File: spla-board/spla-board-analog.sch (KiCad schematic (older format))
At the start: 38 parts, among them J13 J_ANALOG, J14 J_AREF, U4 ADC1173, U5 ADC1173, U6 ADC1173

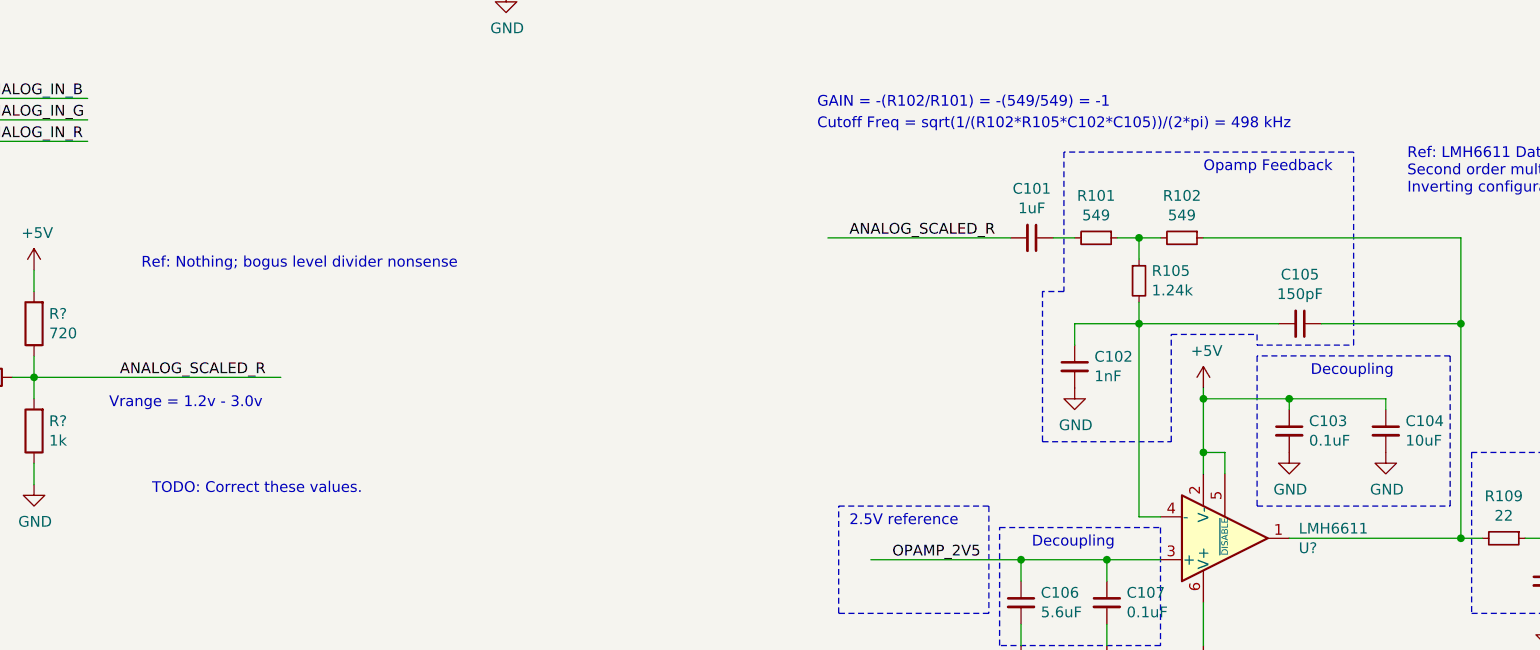
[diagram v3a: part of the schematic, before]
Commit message: schematic: More opamp fiddling.
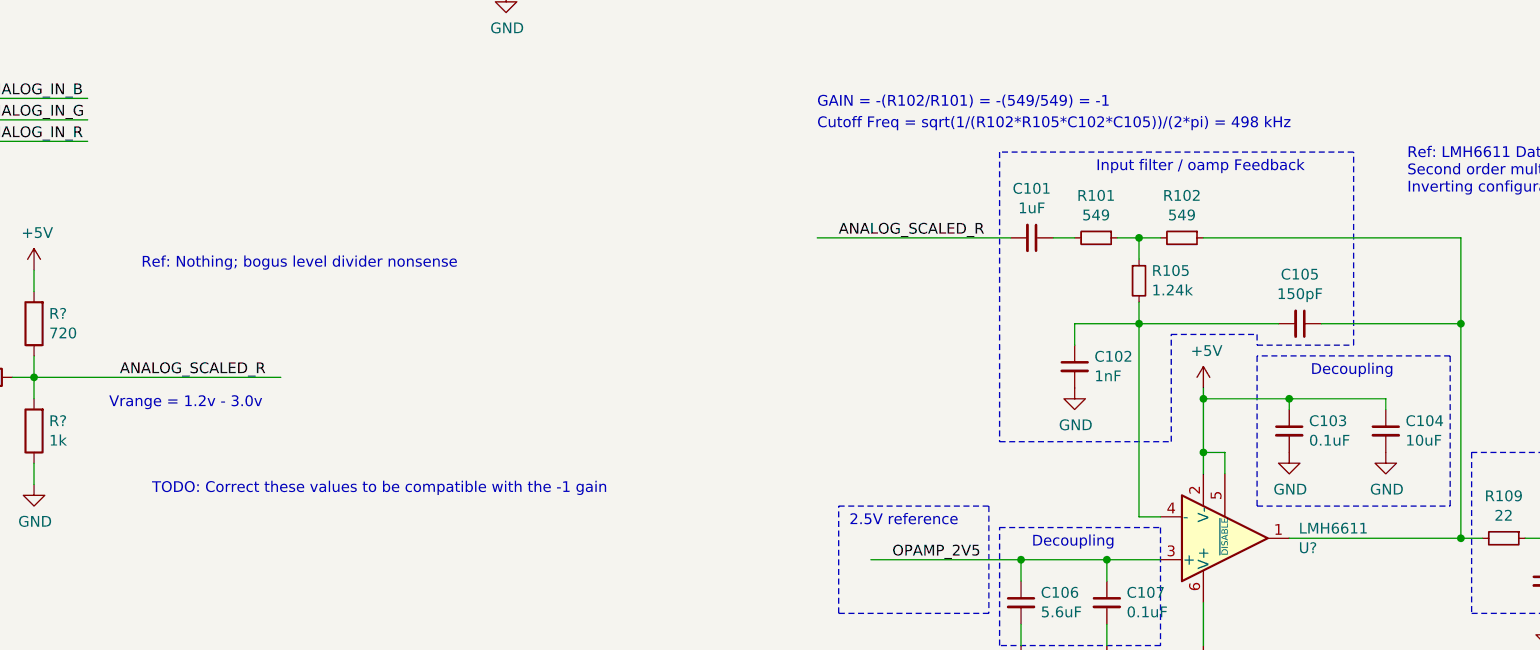
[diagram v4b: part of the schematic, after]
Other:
- note added: "Input filter / oamp Feedback"
- note added: "TODO: Correct these values to be compatible with the -1 gain"
- note removed: "Opamp Feedback"
- note removed: "TODO: Correct these values."
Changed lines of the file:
@@
 Wire Wire Line
 	9800 5650 9800 5550
-Text Label 6550 3850 0    50   ~ 0
+Text Label 6500 3850 0    50   ~ 0
 ANALOG_SCALED_R
 Wire Wire Line
-	6450 3850 7300 3850
+	6400 3850 7300 3850
 Wire Wire Line
 	7500 3850 7600 3850
@@
 	12450 2300 12450 2400
 Text Notes 3300 5050 0    50   ~ 0
-TODO: Correct these values.
+TODO: Correct these values to be compatible with the -1 gain
 Text Notes 7850 2350 0    50   ~ 0
 TODO: Inject opamps to maintain levels
@@
 Cutoff Freq = sqrt(1/(R102*R105*C102*C105))/(2*pi) = 498 kHz
 Wire Notes Line
-	7550 3450 7550 4100
-Wire Notes Line
-	7550 4100 7450 4100
-Wire Notes Line
-	7450 4100 7450 4800
-Wire Notes Line
-	7450 4800 8050 4800
+	7250 4800 8050 4800
 Wire Notes Line
 	8050 4800 8050 4300
@@
 	8900 4350 8900 3450
 Wire Notes Line
-	8900 3450 7550 3450
-Text Notes 8200 3550 0    50   ~ 0
-Opamp Feedback
+	8900 3450 7250 3450
+Text Notes 7700 3550 0    50   ~ 0
+Input filter / oamp Feedback
+Wire Notes Line
+	7250 3450 7250 4800
 $EndSCHEMATC

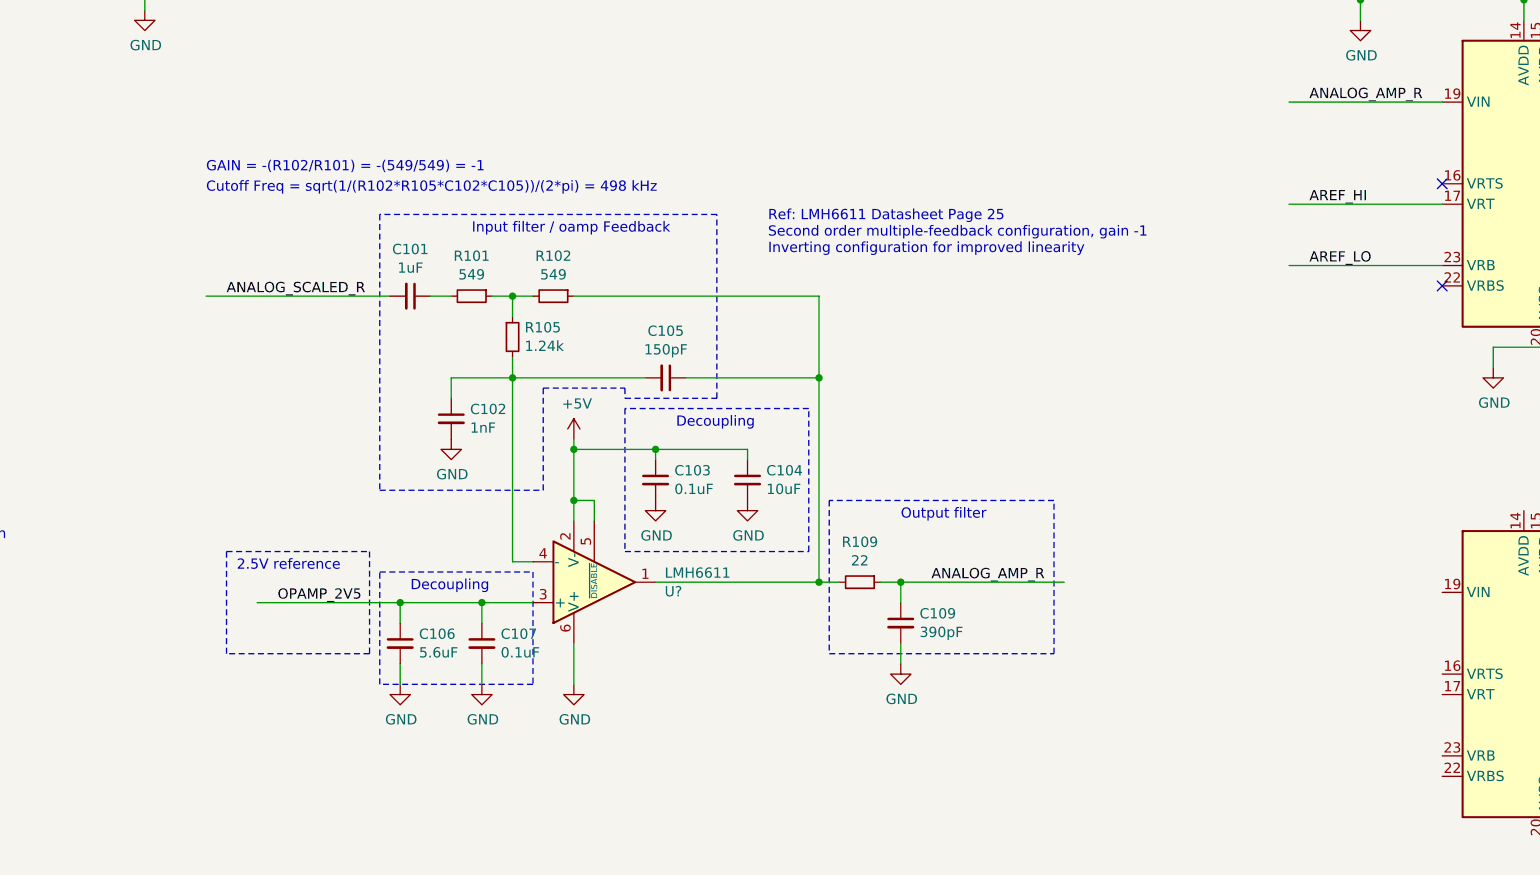
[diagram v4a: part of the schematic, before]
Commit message: schematic: More opamp fiddling.
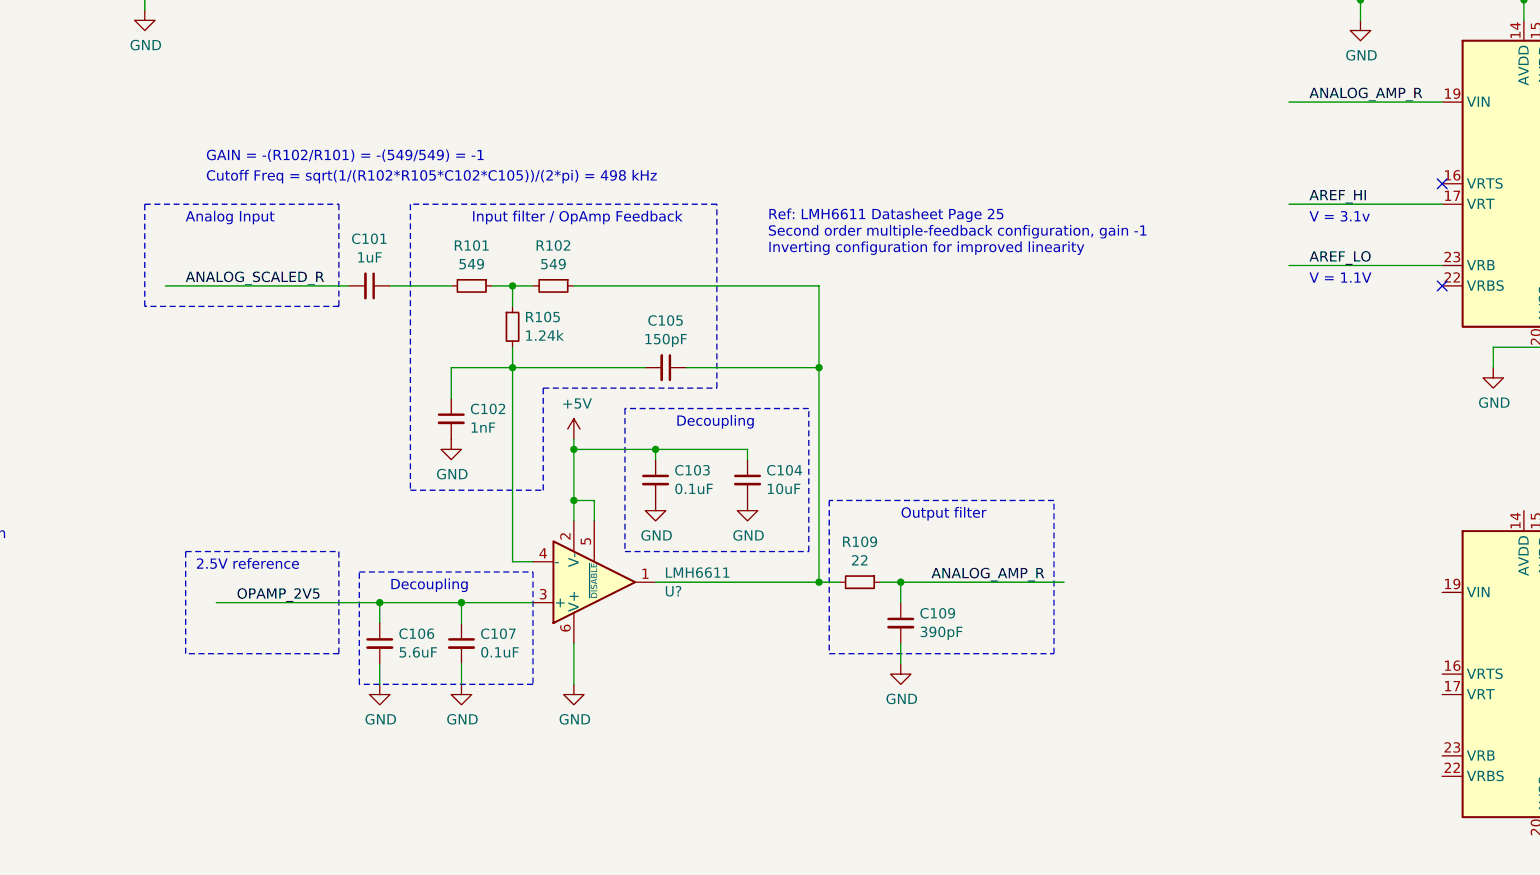
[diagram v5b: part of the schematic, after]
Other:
- note added: "Analog Input"
- note added: "Input filter / OpAmp Feedback"
- note added: "V = 1.1V"
- note added: "V = 3.1v"
- note removed: "Input filter / oamp Feedback"
- moved on the sheet: C101, C105, C106, C107, R101, R102, R105
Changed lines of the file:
@@
 L Device:C_Small C105
 U 1 1 5E9ACDDD
-P 8650 4250
-F 0 "C105" V 8421 4250 50  0000 C CNN
-F 1 "150pF" V 8512 4250 50  0000 C CNN
-F 2 "" H 8650 4250 50  0001 C CNN
-F 3 "~" H 8650 4250 50  0001 C CNN
-	1    8650 4250
+P 8650 4200
+F 0 "C105" V 8421 4200 50  0000 C CNN
+F 1 "150pF" V 8512 4200 50  0000 C CNN
+F 2 "" H 8650 4200 50  0001 C CNN
+F 3 "~" H 8650 4200 50  0001 C CNN
+	1    8650 4200
 	0    1    1    0
 $EndComp
@@
 L Device:C_Small C106
 U 1 1 5E9AE271
-P 7350 5550
-F 0 "C106" H 7442 5596 50  0000 L CNN
-F 1 "5.6uF" H 7442 5505 50  0000 L CNN
-F 2 "" H 7350 5550 50  0001 C CNN
-F 3 "~" H 7350 5550 50  0001 C CNN
-	1    7350 5550
+P 7250 5550
+F 0 "C106" H 7342 5596 50  0000 L CNN
+F 1 "5.6uF" H 7342 5505 50  0000 L CNN
+F 2 "" H 7250 5550 50  0001 C CNN
+F 3 "~" H 7250 5550 50  0001 C CNN
+	1    7250 5550
 	1    0    0    -1
 $EndComp
@@
 L Device:C_Small C107
 U 1 1 5E9AE27B
-P 7750 5550
-F 0 "C107" H 7842 5596 50  0000 L CNN
-F 1 "0.1uF" H 7842 5505 50  0000 L CNN
-F 2 "" H 7750 5550 50  0001 C CNN
-F 3 "~" H 7750 5550 50  0001 C CNN
-	1    7750 5550
+P 7650 5550
+F 0 "C107" H 7742 5596 50  0000 L CNN
+F 1 "0.1uF" H 7742 5505 50  0000 L CNN
+F 2 "" H 7650 5550 50  0001 C CNN
+F 3 "~" H 7650 5550 50  0001 C CNN
+	1    7650 5550
 	1    0    0    -1
 $EndComp
@@
 L Device:R_Small R102
 U 1 1 5E9B8A3B
-P 8100 3850
-F 0 "R102" V 7904 3850 50  0000 C CNN
-F 1 "549" V 7995 3850 50  0000 C CNN
-F 2 "" H 8100 3850 50  0001 C CNN
-F 3 "~" H 8100 3850 50  0001 C CNN
-	1    8100 3850
+P 8100 3800
+F 0 "R102" V 7904 3800 50  0000 C CNN
+F 1 "549" V 7995 3800 50  0000 C CNN
+F 2 "" H 8100 3800 50  0001 C CNN
+F 3 "~" H 8100 3800 50  0001 C CNN
+	1    8100 3800
 	0    1    1    0
 $EndComp
@@
 L Device:R_Small R101
 U 1 1 5E9B9EA4
-P 7700 3850
-F 0 "R101" V 7504 3850 50  0000 C CNN
-F 1 "549" V 7595 3850 50  0000 C CNN
-F 2 "" H 7700 3850 50  0001 C CNN
-F 3 "~" H 7700 3850 50  0001 C CNN
-	1    7700 3850
+P 7700 3800
+F 0 "R101" V 7504 3800 50  0000 C CNN
+F 1 "549" V 7595 3800 50  0000 C CNN
+F 2 "" H 7700 3800 50  0001 C CNN
+F 3 "~" H 7700 3800 50  0001 C CNN
+	1    7700 3800
 	0    1    1    0
 $EndComp
@@
 L Device:C_Small C101
 U 1 1 5E9BBA79
-P 7400 3850
-F 0 "C101" V 7171 3850 50  0000 C CNN
-F 1 "1uF" V 7262 3850 50  0000 C CNN
-F 2 "" H 7400 3850 50  0001 C CNN
-F 3 "~" H 7400 3850 50  0001 C CNN
-	1    7400 3850
+P 7200 3800
+F 0 "C101" V 6971 3800 50  0000 C CNN
+F 1 "1uF" V 7062 3800 50  0000 C CNN
+F 2 "" H 7200 3800 50  0001 C CNN
+F 3 "~" H 7200 3800 50  0001 C CNN
+	1    7200 3800
 	0    1    1    0
 $EndComp
 Wire Wire Line
-	8750 4250 9400 4250
-Wire Wire Line
-	9400 4250 9400 5250
+	8750 4200 9400 4200
+Wire Wire Line
+	9400 4200 9400 5250
 Wire Wire Line
 	9400 5250 8600 5250
 Wire Wire Line
-	8550 4250 7900 4250
-Wire Wire Line
-	7900 4250 7900 5150
+	8550 4200 7900 4200
+Wire Wire Line
+	7900 4200 7900 5150
 Wire Wire Line
 	7900 5150 8000 5150
-Connection ~ 7900 4250
-Wire Wire Line
-	7600 4250 7600 4350
+Connection ~ 7900 4200
+Wire Wire Line
+	7600 4200 7600 4350
 $Comp
 L power:GND #PWR0211
@@
 L power:GND #PWR0217
 U 1 1 5E9F0655
-P 7350 5750
-F 0 "#PWR0217" H 7350 5500 50  0001 C CNN
-F 1 "GND" H 7355 5577 50  0000 C CNN
-F 2 "" H 7350 5750 50  0001 C CNN
-F 3 "" H 7350 5750 50  0001 C CNN
-	1    7350 5750
+P 7250 5750
+F 0 "#PWR0217" H 7250 5500 50  0001 C CNN
+F 1 "GND" H 7255 5577 50  0000 C CNN
+F 2 "" H 7250 5750 50  0001 C CNN
+F 3 "" H 7250 5750 50  0001 C CNN
+	1    7250 5750
 	1    0    0    -1
 $EndComp
@@
 L power:GND #PWR0218
 U 1 1 5E9F2D31
-P 7750 5750
-F 0 "#PWR0218" H 7750 5500 50  0001 C CNN
-F 1 "GND" H 7755 5577 50  0000 C CNN
-F 2 "" H 7750 5750 50  0001 C CNN
-F 3 "" H 7750 5750 50  0001 C CNN
-	1    7750 5750
-	1    0    0    -1
-$EndComp
-Wire Wire Line
-	7750 5350 7750 5450
-Connection ~ 7750 5350
-Wire Wire Line
-	7750 5350 8000 5350
-Wire Wire Line
-	7350 5450 7350 5350
-Wire Wire Line
-	7350 5350 7750 5350
+P 7650 5750
+F 0 "#PWR0218" H 7650 5500 50  0001 C CNN
+F 1 "GND" H 7655 5577 50  0000 C CNN
+F 2 "" H 7650 5750 50  0001 C CNN
+F 3 "" H 7650 5750 50  0001 C CNN
+	1    7650 5750
+	1    0    0    -1
+$EndComp
+Wire Wire Line
+	7650 5350 7650 5450
+Connection ~ 7650 5350
+Wire Wire Line
+	7650 5350 8000 5350
 Wire Wire Line
 	1200 6250 1200 6350
@@
 Wire Wire Line
 	9800 5650 9800 5550
-Text Label 6500 3850 0    50   ~ 0
+Text Label 6300 3800 0    50   ~ 0
 ANALOG_SCALED_R
 Wire Wire Line
-	6400 3850 7300 3850
-Wire Wire Line
-	7500 3850 7600 3850
-Wire Wire Line
-	8200 3850 9400 3850
-Wire Wire Line
-	9400 3850 9400 4250
-Connection ~ 9400 4250
+	6200 3800 7100 3800
+Wire Wire Line
+	7300 3800 7600 3800
+Wire Wire Line
+	8200 3800 9400 3800
+Wire Wire Line
+	9400 3800 9400 4200
+Connection ~ 9400 4200
 Wire Wire Line
 	1200 6250 1400 6250
@@
 ANALOG_AMP_R
 Wire Wire Line
-	7350 5650 7350 5750
-Wire Wire Line
-	7750 5650 7750 5750
+	7250 5650 7250 5750
+Wire Wire Line
+	7650 5650 7650 5750
 Wire Wire Line
 	8200 5550 8200 5750
@@
 Text Label 2800 6250 0    50   ~ 0
 OPAMP_2V5
-Text Label 6750 5350 0    50   ~ 0
-OPAMP_2V5
-Wire Wire Line
-	7350 5350 6650 5350
-Connection ~ 7350 5350
 Wire Wire Line
 	12050 2000 12450 2000
@@
 L Device:R_Small R105
 U 1 1 5E9577DD
-P 7900 4050
-F 0 "R105" H 7959 4096 50  0000 L CNN
-F 1 "1.24k" H 7959 4005 50  0000 L CNN
-F 2 "" H 7900 4050 50  0001 C CNN
-F 3 "~" H 7900 4050 50  0001 C CNN
-	1    7900 4050
-	1    0    0    -1
-$EndComp
-Wire Wire Line
-	7900 3850 7900 3950
-Connection ~ 7900 3850
-Wire Wire Line
-	7900 3850 8000 3850
-Wire Wire Line
-	7600 4250 7900 4250
-Wire Wire Line
-	7800 3850 7900 3850
-Wire Wire Line
-	7900 4150 7900 4250
+P 7900 4000
+F 0 "R105" H 7959 4046 50  0000 L CNN
+F 1 "1.24k" H 7959 3955 50  0000 L CNN
+F 2 "" H 7900 4000 50  0001 C CNN
+F 3 "~" H 7900 4000 50  0001 C CNN
+	1    7900 4000
+	1    0    0    -1
+$EndComp
+Wire Wire Line
+	7900 3800 7900 3900
+Connection ~ 7900 3800
+Wire Wire Line
+	7900 3800 8000 3800
+Wire Wire Line
+	7600 4200 7900 4200
+Wire Wire Line
+	7800 3800 7900 3800
+Wire Wire Line
+	7900 4100 7900 4200
 Wire Notes Line
 	8450 4400 8450 5100
@@
 	9350 4400 8450 4400
 Wire Notes Line
-	7250 5200 8000 5200
+	7150 5200 8000 5200
 Wire Notes Line
 	8000 5200 8000 5750
 Wire Notes Line
-	8000 5750 7250 5750
-Wire Notes Line
-	7250 5750 7250 5200
-Wire Notes Line
-	6500 5100 7200 5100
-Wire Notes Line
-	7200 5100 7200 5600
-Wire Notes Line
-	7200 5600 6500 5600
-Wire Notes Line
-	6500 5600 6500 5100
+	8000 5750 7150 5750
+Wire Notes Line
+	7150 5750 7150 5200
+Wire Notes Line
+	6300 5600 6300 5100
 Wire Notes Line
 	9450 4850 9450 5600
@@
 Text Notes 8700 4500 0    50   ~ 0
 Decoupling
-Text Notes 7400 5300 0    50   ~ 0
+Text Notes 7300 5300 0    50   ~ 0
 Decoupling
-Text Notes 6550 5200 0    50   ~ 0
+Text Notes 6350 5200 0    50   ~ 0
 2.5V reference
-Text Notes 6400 3250 0    50   ~ 0
+Text Notes 6400 3200 0    50   ~ 0
 GAIN = -(R102/R101) = -(549/549) = -1
-Text Notes 6400 3350 0    50   ~ 0
+Text Notes 6400 3300 0    50   ~ 0
 Cutoff Freq = sqrt(1/(R102*R105*C102*C105))/(2*pi) = 498 kHz
 Wire Notes Line
-	7250 4800 8050 4800
+	7400 4800 8050 4800
 Wire Notes Line
 	8050 4800 8050 4300
 Wire Notes Line
-	8050 4300 8450 4300
-Wire Notes Line
-	8450 4300 8450 4350
-Wire Notes Line
-	8450 4350 8900 4350
-Wire Notes Line
-	8900 4350 8900 3450
-Wire Notes Line
-	8900 3450 7250 3450
-Text Notes 7700 3550 0    50   ~ 0
-Input filter / oamp Feedback
-Wire Notes Line
-	7250 3450 7250 4800
+	8900 4300 8900 3400
+Wire Notes Line
+	8900 3400 7400 3400
+Text Notes 7700 3500 0    50   ~ 0
+Input filter / OpAmp Feedback
+Wire Notes Line
+	7400 3400 7400 4800
+Text Notes 11800 3500 0    50   ~ 0
+V = 3.1v
+Text Notes 11800 3800 0    50   ~ 0
+V = 1.1V
+Wire Notes Line
+	8050 4300 8900 4300
+Connection ~ 7250 5350
+Text Label 6550 5350 0    50   ~ 0
+OPAMP_2V5
+Wire Wire Line
+	7250 5350 7650 5350
+Wire Wire Line
+	7250 5450 7250 5350
+Wire Notes Line
+	7050 5600 6300 5600
+Wire Notes Line
+	7050 5100 7050 5600
+Wire Notes Line
+	6300 5100 7050 5100
+Wire Wire Line
+	7250 5350 6450 5350
+Wire Notes Line
+	6100 3400 7050 3400
+Wire Notes Line
+	7050 3400 7050 3900
+Wire Notes Line
+	7050 3900 6100 3900
+Wire Notes Line
+	6100 3900 6100 3400
+Text Notes 6300 3500 0    50   ~ 0
+Analog Input
 $EndSCHEMATC
